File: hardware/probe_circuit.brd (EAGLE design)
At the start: 47.9 x 35.5 mm, 15 parts, among them J1 VPD, J2 VSIG, J3 VLED, J4 VOFF, J5 VPD, J6 VSIG, J7 VCC_IN, J8 0-5k, J9 0-10k, U1 LT1920CS8PBF

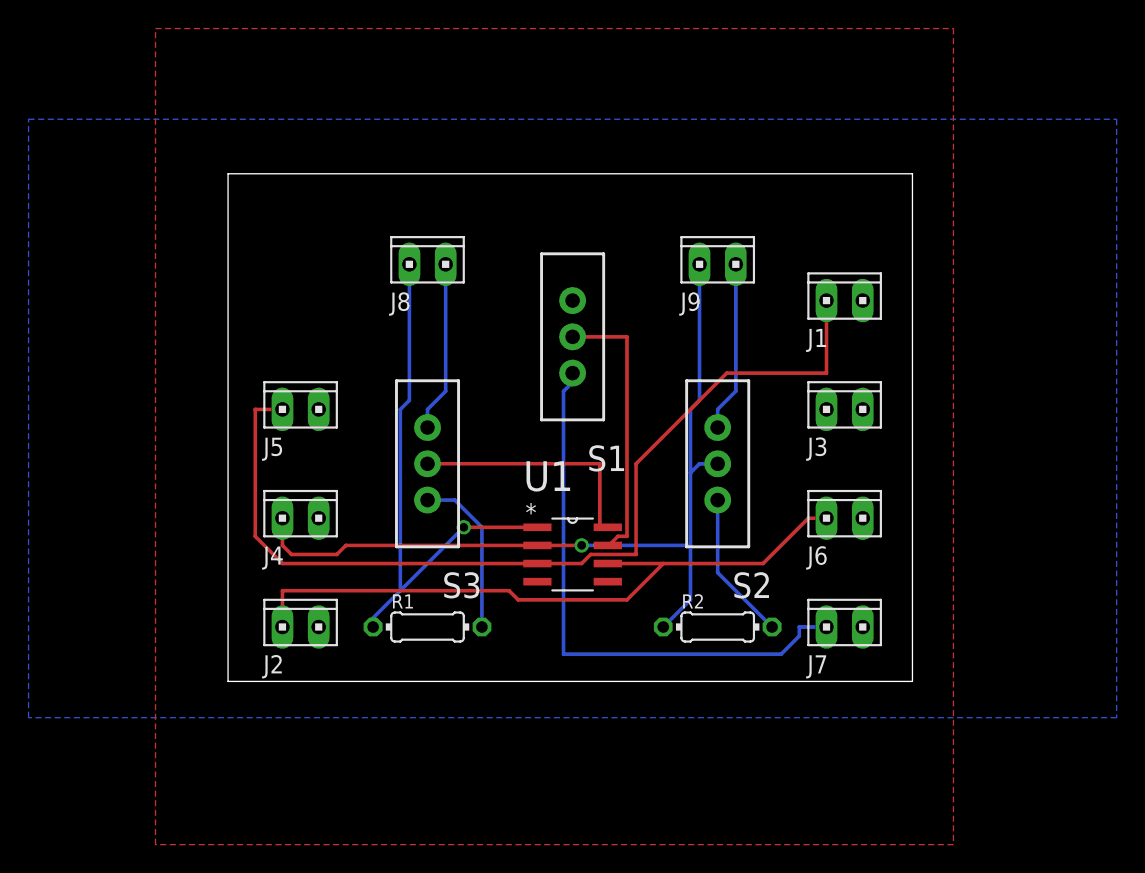
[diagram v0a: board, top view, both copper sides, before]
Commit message: Connected VLED to VCC via resistor.  Amended polygon area.
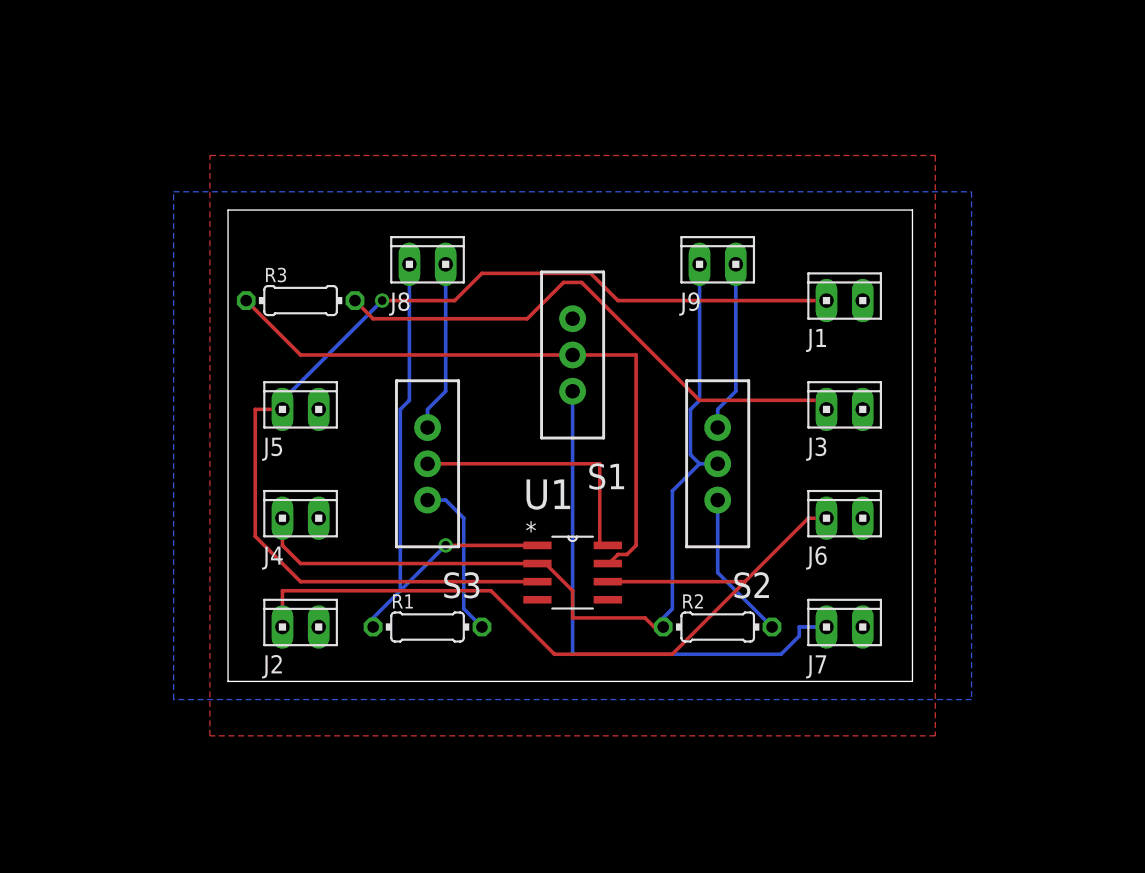
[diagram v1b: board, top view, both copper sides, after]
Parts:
- added R3: R_LED, eagle-ltspice:0204/7
- moved U1 1.27 mm to (24.1, 7.62)
- moved S1 1.27 mm to (24.1, 22.9)
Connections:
- net VCC: now also R3.1
- net VLED: now also R3.2
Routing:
- net VLED: track 0.00 -> 38.3 mm
- net VCC: track 19.4 -> 44.7 mm
- net VPD: track 65.9 -> 75.1 mm, vias 0 -> 1
- net VSIG: track 47.2 -> 56.0 mm
- net VCC_IN: track 39.5 -> 37.4 mm
- net RG_X: track 17.1 -> 18.3 mm
- net VOFF: track 59.6 -> 60.3 mm, vias 1 -> 0
- net RG: track 37.9 -> 37.4 mm
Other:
- board size 47.9 x 35.5 mm -> 47.9 x 33 mm
